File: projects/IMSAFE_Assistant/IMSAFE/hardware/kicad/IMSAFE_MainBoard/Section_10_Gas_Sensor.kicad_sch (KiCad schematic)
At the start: 0 parts

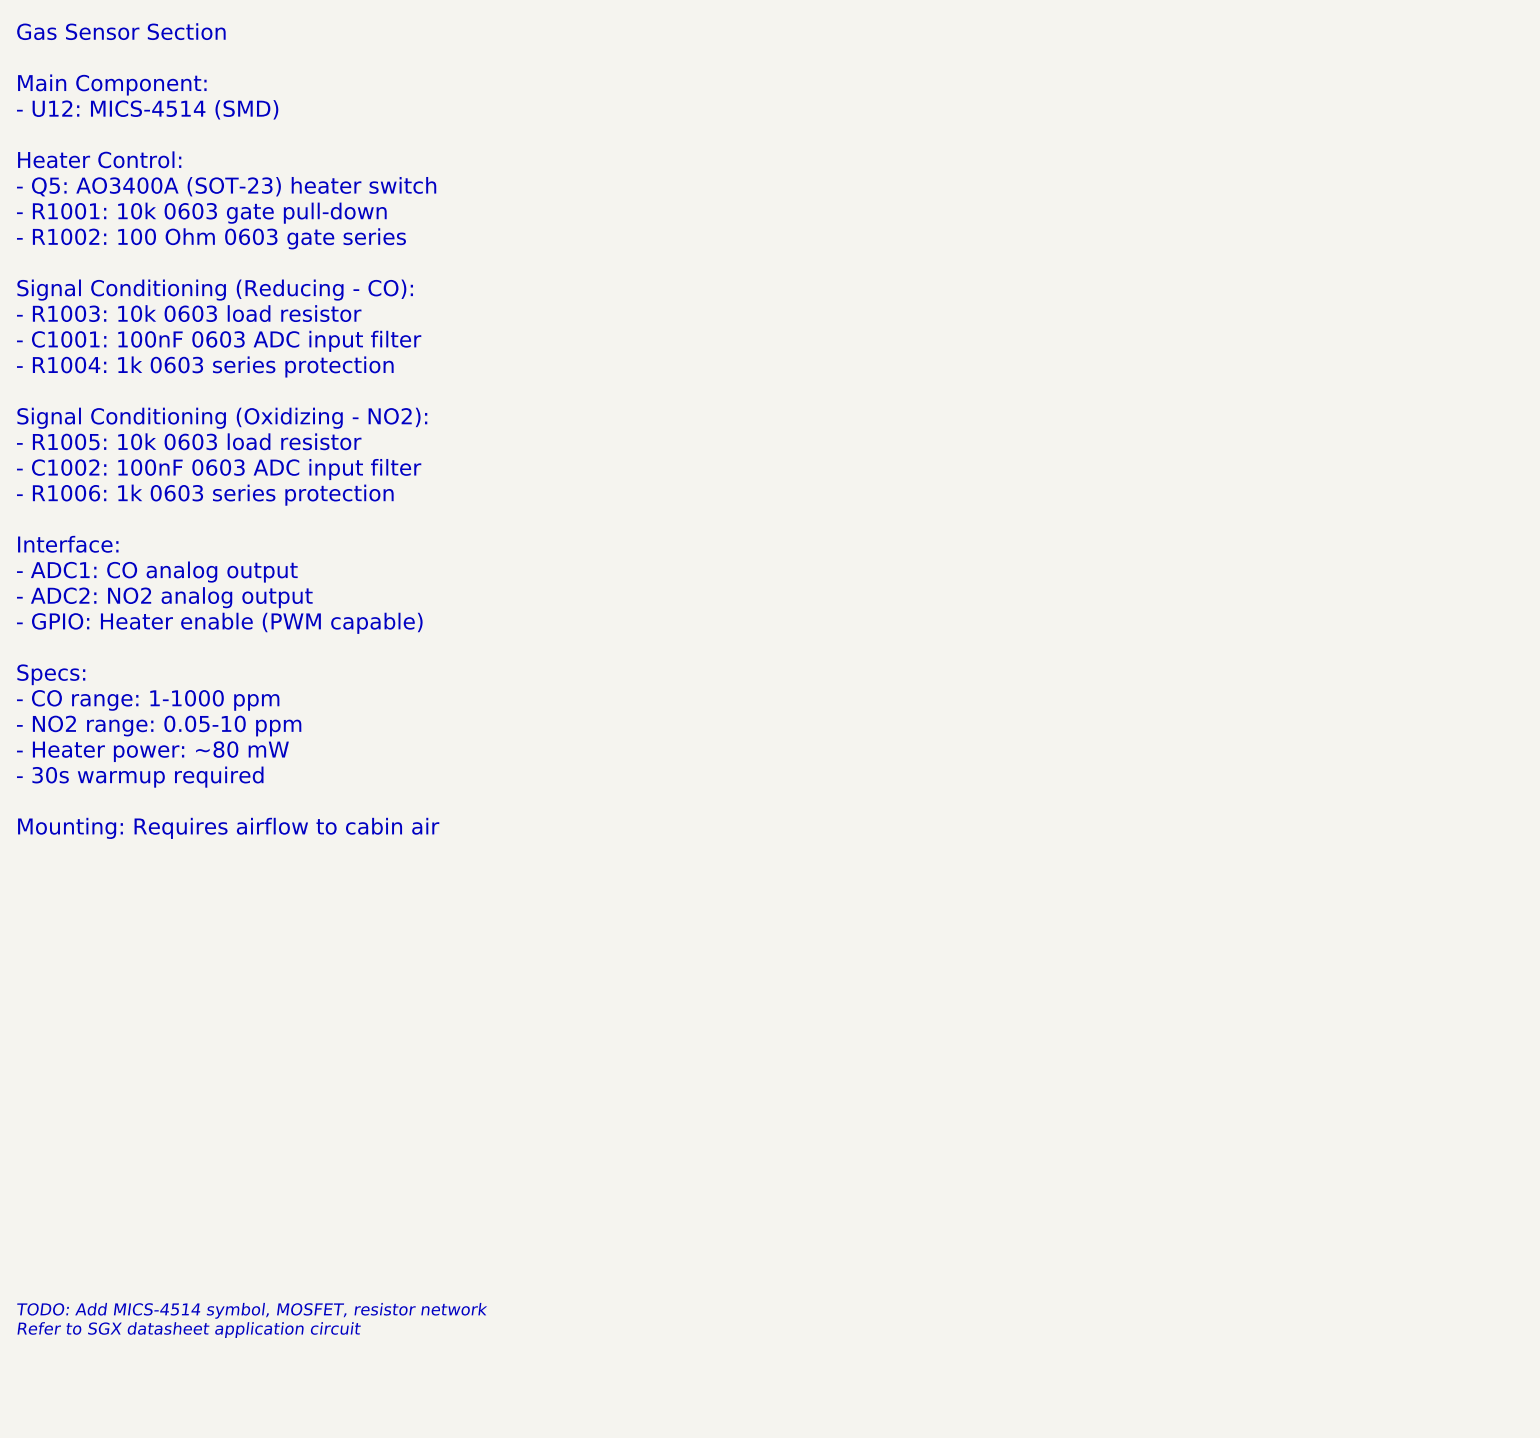
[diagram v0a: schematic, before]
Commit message: Add sensor and interface schematic implementations
- Section 01: MCU Core additional connections
- Section 04: BMS refinements
- Section 07: Barometric sensor (BMP390)
- Section 08: IMU (ICM-42688-P) full implementation
- Section 09: Magnetometer (MMC5983MA) full implementation
- Section 10: Gas sensor (MICS-4514) with heater control
- Section 11: Temp/Humidity (Si7021-A20) implementation
- Section 14: I/O Expander updates
- Section 16: Rotary encoder connections
- Section 19: Audio buzzer (MLT-8530) with MOSFET driver

Co-Authored-By: Claude Opus 4.5 <noreply@anthropic.com>
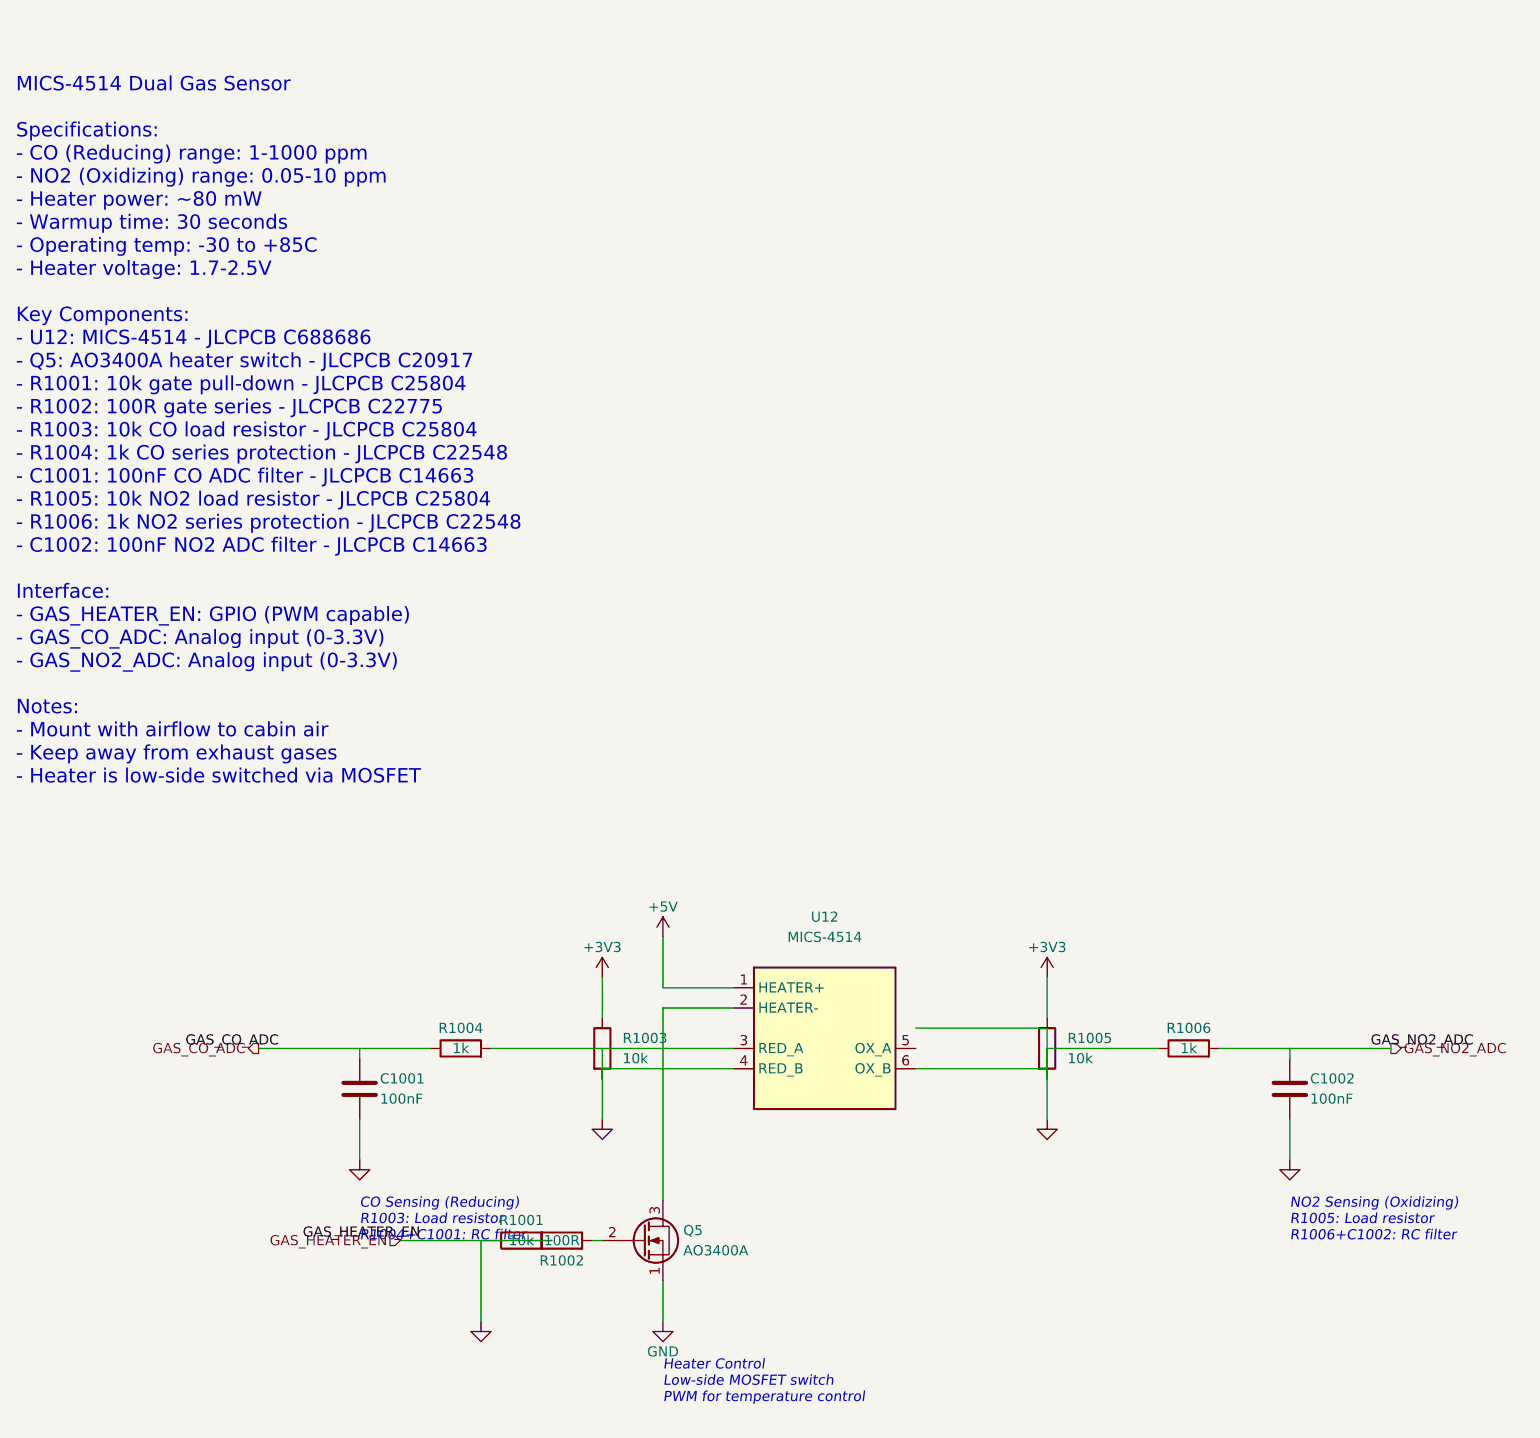
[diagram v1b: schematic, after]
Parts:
- added C1001, C1002: 100nF, Capacitor_SMD:C_0603_1608Metric, symbol Device:C
- added Q5: AO3400A, Package_TO_SOT_SMD:SOT-23, symbol Transistor_FET:AO3400A
- added R1001, R1003, R1005: 10k, Resistor_SMD:R_0603_1608Metric, symbol Device:R
- added R1002: 100R, Resistor_SMD:R_0603_1608Metric, symbol Device:R
- added R1004, R1006: 1k, Resistor_SMD:R_0603_1608Metric, symbol Device:R
- added U12: MICS-4514, Sensor_Gas:SGX_MICS-4514, symbol Sensor_Gas:MICS-4514
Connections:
- new net: Q5.2 (G), R1002.2
- new net: Q5.3 (D), U12.2 (HEATER-)
- new net +3V3: R1003.1, R1005.1
- new net +5V: U12.1 (HEATER+)
- new net GAS_CO_ADC: C1001.1, R1004.1
- new net GAS_NO2_ADC: C1002.1, R1006.2
- new net GND: C1001.2, C1002.2, Q5.1 (S), R1001.1, R1001.2, R1002.1, R1003.2, R1004.2, R1005.2, R1006.1, U12.3 (RED_A), U12.4 (RED_B), U12.6 (OX_B)
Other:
- note added: "CO Sensing (Reducing) R1003: Load resistor R1004+C1001: RC filter"
- note added: "Heater Control Low-side MOSFET switch PWM for temperature control"
- note added: "MICS-4514 Dual Gas Sensor Specifications: - CO (Reducing) range: 1-1000 ppm - NO2 (Oxidizing) range: 0.05-10 ppm - Heater power: ~80 mW - Warmup time: 30 seconds - Operating temp: -30 to +85C - Heater voltage: 1.7-2.5V Key Components: - U12: MICS-4514 - JLCPCB C688686 - Q5: AO3400A heater switch - JLCPCB C20917 - R1001: 10k gate pull-down - JLCPCB C25804 - R1002: 100R gate series - JLCPCB C22775 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"
- note added: "NO2 Sensing (Oxidizing) R1005: Load resistor R1006+C1002: RC filter"
- note removed: "Gas Sensor Section Main Component: - U12: MICS-4514 (SMD) Heater Control: - Q5: AO3400A (SOT-23) heater switch - R1001: 10k 0603 gate pull-down - R1002: 100 Ohm 0603 gate series Signal Conditioning (Reducing - CO): - R1003: 10k 0603 load resistor - C1001: 100nF 0603 ADC input filter - R1004: 1k 0603 series protection Signal Conditioning (Oxidizing - NO2): - R1005: 10k 0603 load resistor - C1002: 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"
- note removed: "TODO: Add MICS-4514 symbol, MOSFET, resistor network Refer to SGX datasheet application circuit"

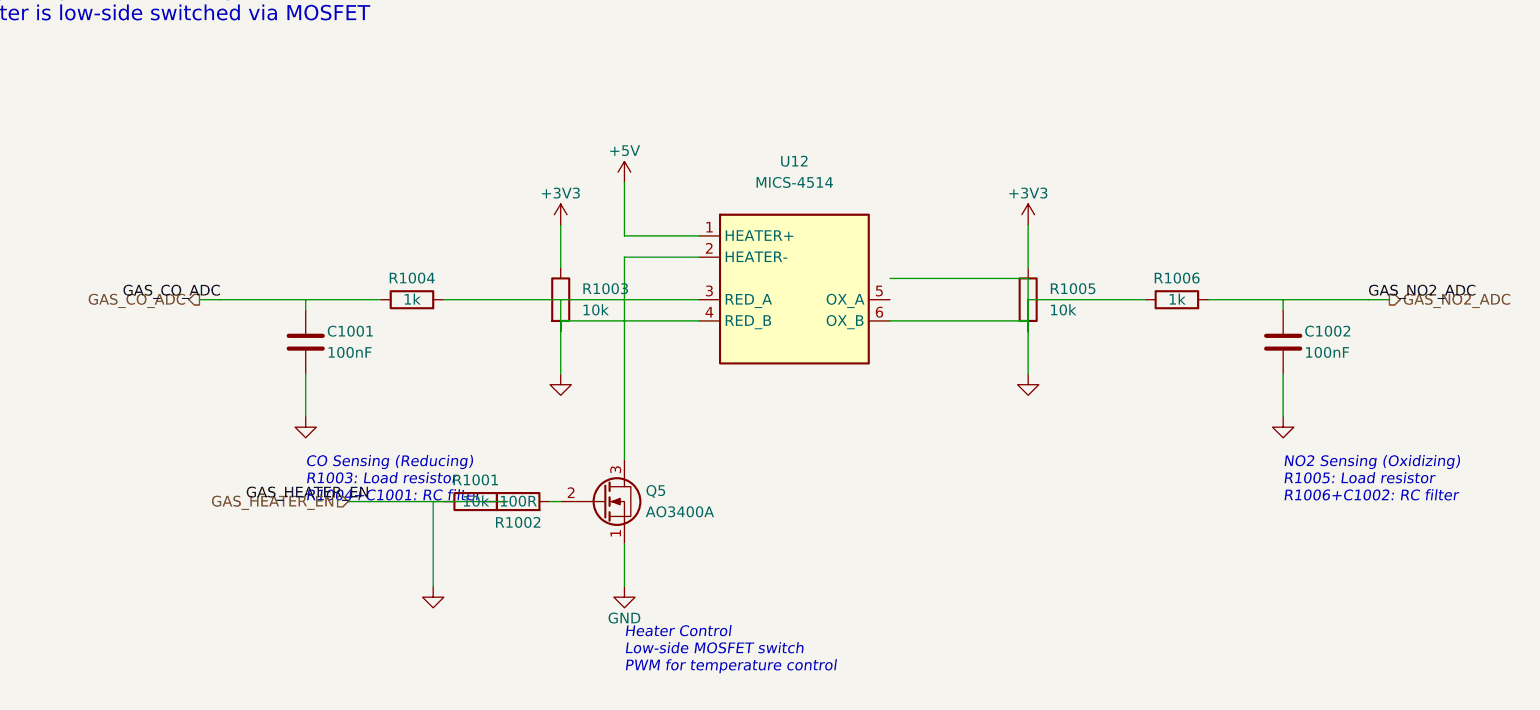
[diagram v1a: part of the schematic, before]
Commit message: Update KiCad schematics and add analysis files
- Update all MainBoard schematic sections with component placement
- Add ERC reports and analysis scripts for schematic validation
- Update Radar Interface and SwitchLED Board projects
- Sync KiCad project files with latest session changes

Co-Authored-By: Claude Opus 4.5 <noreply@anthropic.com>
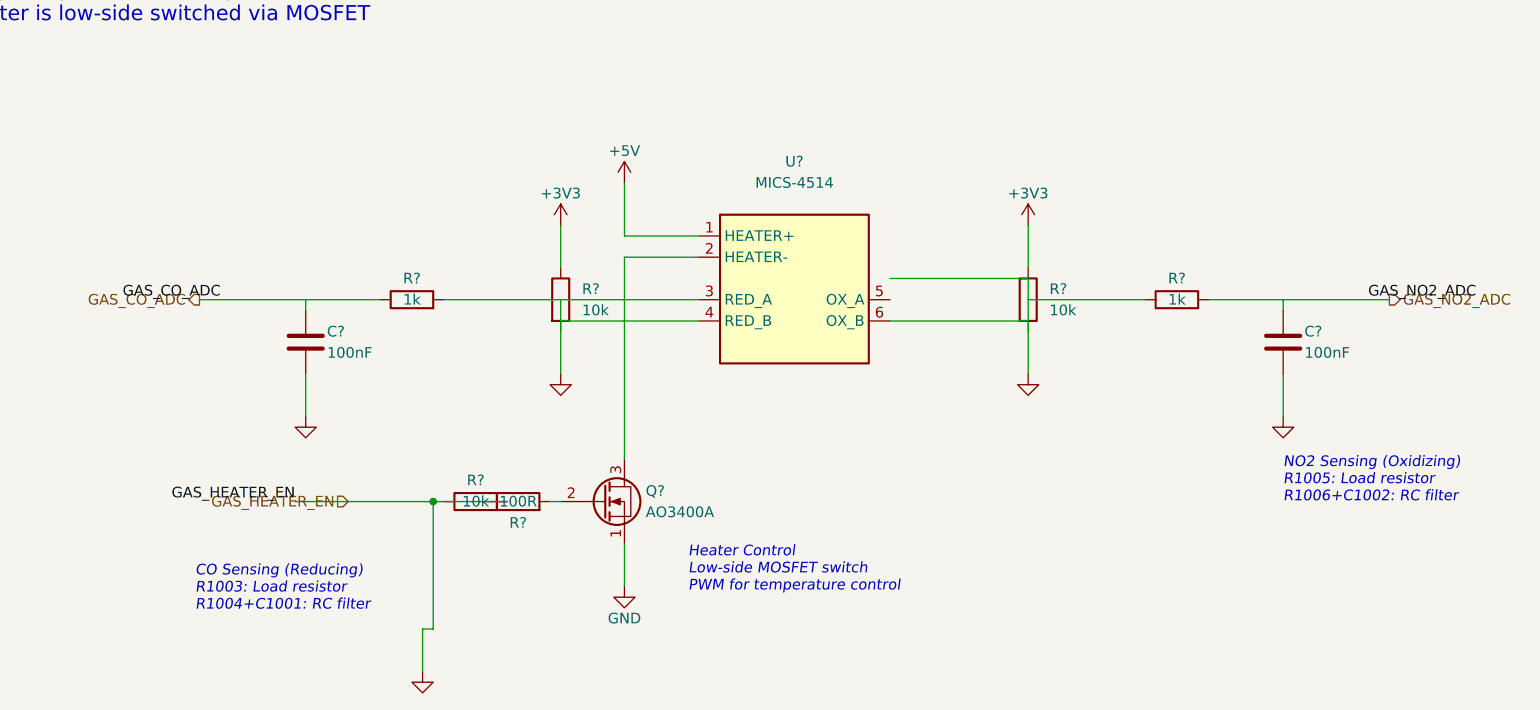
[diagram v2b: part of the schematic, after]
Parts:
- removed C1001, C1002: 100nF, Capacitor_SMD:C_0603_1608Metric, symbol Device:C
- removed Q5: AO3400A, Package_TO_SOT_SMD:SOT-23, symbol Transistor_FET:AO3400A
- removed R1001, R1003, R1005: 10k, Resistor_SMD:R_0603_1608Metric, symbol Device:R
- removed R1002: 100R, Resistor_SMD:R_0603_1608Metric, symbol Device:R
- removed R1004, R1006: 1k, Resistor_SMD:R_0603_1608Metric, symbol Device:R
- removed U12: MICS-4514, Sensor_Gas:SGX_MICS-4514, symbol Sensor_Gas:MICS-4514
- added C? (x2): 100nF, Capacitor_SMD:C_0603_1608Metric, symbol Device:C
- added Q?: AO3400A, Package_TO_SOT_SMD:SOT-23, symbol Transistor_FET:AO3400A
- added R? (x3): 10k, Resistor_SMD:R_0603_1608Metric, symbol Device:R
- added R? (x2): 1k, Resistor_SMD:R_0603_1608Metric, symbol Device:R
- added R?: 100R, Resistor_SMD:R_0603_1608Metric, symbol Device:R
- added U?: MICS-4514, Sensor_Gas:SGX_MICS-4514, symbol Sensor_Gas:MICS-4514
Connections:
- net +3V3: now also R?.1, R?.1
- net +5V: now also U?.1 (HEATER+)
- net GAS_CO_ADC: now also C?.1, R?.1
- net GAS_NO2_ADC: now also C?.1, R?.2
- net GND: now also C?.2, C?.2, Q?.1 (S), R?.1, R?.2, R?.2, U?.3 (RED_A)
- new net: Q?.2 (G), R?.2
- new net: Q?.3 (D), U?.2 (HEATER-)
